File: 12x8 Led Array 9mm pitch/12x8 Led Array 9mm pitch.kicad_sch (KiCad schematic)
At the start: 25 parts, among them J1 LED ch 1-24, J2 LED ch 25-48, J3 LED ch 49-72, J4 LED ch 73-96, J5 logic/analog, U1 CD74HC4067M96, U2 CD74HC4067M96, U3 CD74HC4067M96, U4 CD74HC4067M96, U5 CD74HC4067M96, U6 CD74HC4067M96

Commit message: Swap to 6x 40-pin IDC ribbons (IDE-safe pinout), clear routing for rearrange
- J1-J6 both boards: 16 channels each = one PCA9685 bank per cable;
  pairs on pins 1-18/21-34, pin 20 NC (IDE key), GND 19+35-40
- Logic ribbon renamed J9; control screw terminal now J12
- Schematics regenerated (netlists verified 300+412), CONNECTIONS
  updated; connectors placed at nominal spots for user rearrangement
- All routing cleared except LED thermal via farms per user request
- New vault note: What Every Part Does

Co-Authored-By: Claude Fable 5 <noreply@anthropic.com>
Claude-Session: https://claude.ai/code/session_017oD54uh7Tvu54u9NPQNcZB
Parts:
- added J6: LED ch 81-96, Connector_IDC:IDC-Header_2x20_P2.54mm_Vertical, symbol Connector_Generic:Conn_02x20_Odd_Even
- added J9: logic/analog, Connector_IDC:IDC-Header_2x10_P2.54mm_Horizontal, symbol Connector_Generic:Conn_02x10_Odd_Even
- J1: value LED ch 1-24 -> LED ch 1-16; footprint Connector_IDC:IDC-Header_2x25_P2.54mm_Vertical -> Connector_IDC:IDC-Header_2x20_P2.54mm_Vertical; symbol Connector_Generic:Conn_02x25_Odd_Even -> Connector_Generic:Conn_02x20_Odd_Even; LCSC C9044 -> C9043
- J2: value LED ch 25-48 -> LED ch 17-32; footprint Connector_IDC:IDC-Header_2x25_P2.54mm_Vertical -> Connector_IDC:IDC-Header_2x20_P2.54mm_Vertical; symbol Connector_Generic:Conn_02x25_Odd_Even -> Connector_Generic:Conn_02x20_Odd_Even; LCSC C9044 -> C9043
- J3: value LED ch 49-72 -> LED ch 33-48; footprint Connector_IDC:IDC-Header_2x25_P2.54mm_Vertical -> Connector_IDC:IDC-Header_2x20_P2.54mm_Vertical; symbol Connector_Generic:Conn_02x25_Odd_Even -> Connector_Generic:Conn_02x20_Odd_Even; LCSC C9044 -> C9043
- J4: value LED ch 73-96 -> LED ch 49-64; footprint Connector_IDC:IDC-Header_2x25_P2.54mm_Vertical -> Connector_IDC:IDC-Header_2x20_P2.54mm_Vertical; symbol Connector_Generic:Conn_02x25_Odd_Even -> Connector_Generic:Conn_02x20_Odd_Even; LCSC C9044 -> C9043
- J5: value logic/analog -> LED ch 65-80; footprint Connector_IDC:IDC-Header_2x10_P2.54mm_Horizontal -> Connector_IDC:IDC-Header_2x20_P2.54mm_Vertical; symbol Connector_Generic:Conn_02x10_Odd_Even -> Connector_Generic:Conn_02x20_Odd_Even; LCSC C9144 -> C9043
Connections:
- net +3.3V: now also J9.1 (Pin_1); no longer J5.1 (Pin_1)
- net GND: now also J1.19 (Pin_19), J1.35 (Pin_35), J1.36 (Pin_36), J1.37 (Pin_37), J1.38 (Pin_38), J1.39 (Pin_39), J1.40 (Pin_40), J2.19 (Pin_19), J2.35 (Pin_35), J2.36 (Pin_36), J2.37 (Pin_37), J2.38 (Pin_38), J2.39 (Pin_39), J2.40 (Pin_40), J3.19 (Pin_19), J3.35 (Pin_35), J3.36 (Pin_36), J3.37 (Pin_37), J3.38 (Pin_38), J3.39 (Pin_39), J3.40 (Pin_40), J4.19 (Pin_19), J4.35 (Pin_35), J4.36 (Pin_36), J4.37 (Pin_37), J4.38 (Pin_38), J4.39 (Pin_39), J4.40 (Pin_40), J5.35 (Pin_35), J5.36 (Pin_36), J5.37 (Pin_37), J5.38 (Pin_38), J5.39 (Pin_39), J5.40 (Pin_40), J6.19 (Pin_19), J6.35 (Pin_35), J6.36 (Pin_36), J6.37 (Pin_37), J6.38 (Pin_38), J6.39 (Pin_39), J6.40 (Pin_40), J9.10 (Pin_10), J9.12 (Pin_12), J9.14 (Pin_14), J9.19 (Pin_19), J9.2 (Pin_2), J9.20 (Pin_20), J9.4 (Pin_4), J9.6 (Pin_6), J9.8 (Pin_8); no longer J1.49 (Pin_49), J1.50 (Pin_50), J2.49 (Pin_49), J2.50 (Pin_50), J3.49 (Pin_49), J3.50 (Pin_50), J4.49 (Pin_49), J4.50 (Pin_50), J5.10 (Pin_10), J5.12 (Pin_12), J5.14 (Pin_14), J5.2 (Pin_2), J5.20 (Pin_20), J5.4 (Pin_4), J5.6 (Pin_6), J5.8 (Pin_8)
- net LED_A10: now also J1.21 (Pin_21); no longer J2.25 (Pin_25)
- net LED_A11: now also J1.23 (Pin_23); no longer J2.33 (Pin_33)
- net LED_A12: now also J1.25 (Pin_25); no longer J2.41 (Pin_41)
- net LED_A13: now also J1.27 (Pin_27); no longer J1.3 (Pin_3)
- net LED_A14: now also J1.29 (Pin_29); no longer J1.11 (Pin_11)
- net LED_A15: now also J1.31 (Pin_31); no longer J1.19 (Pin_19)
- net LED_A16: now also J1.33 (Pin_33); no longer J1.27 (Pin_27)
- net LED_A17: now also J2.1 (Pin_1); no longer J1.35 (Pin_35)
- net LED_A18: now also J2.3 (Pin_3); no longer J1.43 (Pin_43)
- net LED_A19: now also J2.5 (Pin_5); no longer J2.3 (Pin_3)
- net LED_A2: now also J1.3 (Pin_3); no longer J1.9 (Pin_9)
- net LED_A20: now also J2.7 (Pin_7); no longer J2.11 (Pin_11)
- net LED_A21: now also J2.9 (Pin_9); no longer J2.19 (Pin_19)
- net LED_A22: now also J2.11 (Pin_11); no longer J2.27 (Pin_27)
- net LED_A23: now also J2.13 (Pin_13); no longer J2.35 (Pin_35)
- net LED_A24: now also J2.15 (Pin_15); no longer J2.43 (Pin_43)
- net LED_A25: now also J2.17 (Pin_17); no longer J1.5 (Pin_5)
- net LED_A26: now also J2.21 (Pin_21); no longer J1.13 (Pin_13)
- net LED_A27: now also J2.23 (Pin_23); no longer J1.21 (Pin_21)
- net LED_A28: now also J2.25 (Pin_25); no longer J1.29 (Pin_29)
- net LED_A29: now also J2.27 (Pin_27); no longer J1.37 (Pin_37)
- net LED_A3: now also J1.5 (Pin_5); no longer J1.17 (Pin_17)
- net LED_A30: now also J2.29 (Pin_29); no longer J1.45 (Pin_45)
- net LED_A31: now also J2.31 (Pin_31); no longer J2.5 (Pin_5)
- net LED_A32: now also J2.33 (Pin_33); no longer J2.13 (Pin_13)
- net LED_A33: now also J3.1 (Pin_1); no longer J2.21 (Pin_21)
- net LED_A34: now also J3.3 (Pin_3); no longer J2.29 (Pin_29)
- net LED_A35: now also J3.5 (Pin_5); no longer J2.37 (Pin_37)
- net LED_A36: now also J3.7 (Pin_7); no longer J2.45 (Pin_45)
- net LED_A37: now also J3.9 (Pin_9); no longer J1.7 (Pin_7)
- net LED_A38: now also J3.11 (Pin_11); no longer J1.15 (Pin_15)
- net LED_A39: now also J3.13 (Pin_13); no longer J1.23 (Pin_23)
- net LED_A4: now also J1.7 (Pin_7); no longer J1.25 (Pin_25)
- net LED_A40: now also J3.15 (Pin_15); no longer J1.31 (Pin_31)
- net LED_A41: now also J3.17 (Pin_17); no longer J1.39 (Pin_39)
- net LED_A42: now also J3.21 (Pin_21); no longer J1.47 (Pin_47)
- net LED_A43: now also J3.23 (Pin_23); no longer J2.7 (Pin_7)
- net LED_A44: now also J3.25 (Pin_25); no longer J2.15 (Pin_15)
- net LED_A45: now also J3.27 (Pin_27); no longer J2.23 (Pin_23)
- net LED_A46: now also J3.29 (Pin_29); no longer J2.31 (Pin_31)
- net LED_A47: now also J3.31 (Pin_31); no longer J2.39 (Pin_39)
- net LED_A48: now also J3.33 (Pin_33); no longer J2.47 (Pin_47)
- net LED_A5: now also J1.9 (Pin_9); no longer J1.33 (Pin_33)
- net LED_A50: now also J4.3 (Pin_3); no longer J4.9 (Pin_9)
- net LED_A51: now also J4.5 (Pin_5); no longer J4.17 (Pin_17)
- net LED_A52: now also J4.7 (Pin_7); no longer J4.25 (Pin_25)
- net LED_A53: now also J4.9 (Pin_9); no longer J4.33 (Pin_33)
- net LED_A54: now also J4.11 (Pin_11); no longer J4.41 (Pin_41)
- net LED_A55: now also J4.13 (Pin_13); no longer J3.1 (Pin_1)
- net LED_A56: now also J4.15 (Pin_15); no longer J3.9 (Pin_9)
- net LED_A57: now also J4.17 (Pin_17); no longer J3.17 (Pin_17)
- net LED_A58: now also J4.21 (Pin_21); no longer J3.25 (Pin_25)
- net LED_A59: now also J4.23 (Pin_23); no longer J3.33 (Pin_33)
- net LED_A6: now also J1.11 (Pin_11); no longer J1.41 (Pin_41)
- net LED_A60: now also J4.25 (Pin_25); no longer J3.41 (Pin_41)
- net LED_A61: now also J4.27 (Pin_27); no longer J4.3 (Pin_3)
- net LED_A62: now also J4.29 (Pin_29); no longer J4.11 (Pin_11)
- net LED_A63: now also J4.31 (Pin_31); no longer J4.19 (Pin_19)
- net LED_A64: now also J4.33 (Pin_33); no longer J4.27 (Pin_27)
- net LED_A65: now also J5.1 (Pin_1); no longer J4.35 (Pin_35)
- net LED_A66: now also J5.3 (Pin_3); no longer J4.43 (Pin_43)
- net LED_A67: now also J5.5 (Pin_5); no longer J3.3 (Pin_3)
- net LED_A68: now also J5.7 (Pin_7); no longer J3.11 (Pin_11)
- net LED_A69: now also J5.9 (Pin_9); no longer J3.19 (Pin_19)
- net LED_A7: now also J1.13 (Pin_13); no longer J2.1 (Pin_1)
- net LED_A70: now also J5.11 (Pin_11); no longer J3.27 (Pin_27)
- net LED_A71: now also J5.13 (Pin_13); no longer J3.35 (Pin_35)
- net LED_A72: now also J5.15 (Pin_15); no longer J3.43 (Pin_43)
- net LED_A73: now also J5.17 (Pin_17); no longer J4.5 (Pin_5)
- net LED_A74: now also J5.21 (Pin_21); no longer J4.13 (Pin_13)
- net LED_A75: now also J5.23 (Pin_23); no longer J4.21 (Pin_21)
- net LED_A76: now also J5.25 (Pin_25); no longer J4.29 (Pin_29)
- net LED_A77: now also J5.27 (Pin_27); no longer J4.37 (Pin_37)
- net LED_A78: now also J5.29 (Pin_29); no longer J4.45 (Pin_45)
- net LED_A79: now also J5.31 (Pin_31); no longer J3.5 (Pin_5)
- net LED_A8: now also J1.15 (Pin_15); no longer J2.9 (Pin_9)
- net LED_A80: now also J5.33 (Pin_33); no longer J3.13 (Pin_13)
- net LED_A81: now also J6.1 (Pin_1); no longer J3.21 (Pin_21)
- net LED_A82: now also J6.3 (Pin_3); no longer J3.29 (Pin_29)
- net LED_A83: now also J6.5 (Pin_5); no longer J3.37 (Pin_37)
- net LED_A84: now also J6.7 (Pin_7); no longer J3.45 (Pin_45)
- net LED_A85: now also J6.9 (Pin_9); no longer J4.7 (Pin_7)
- net LED_A86: now also J6.11 (Pin_11); no longer J4.15 (Pin_15)
- net LED_A87: now also J6.13 (Pin_13); no longer J4.23 (Pin_23)
- net LED_A88: now also J6.15 (Pin_15); no longer J4.31 (Pin_31)
- net LED_A89: now also J6.17 (Pin_17); no longer J4.39 (Pin_39)
- net LED_A9: now also J1.17 (Pin_17); no longer J2.17 (Pin_17)
- net LED_A90: now also J6.21 (Pin_21); no longer J4.47 (Pin_47)
- net LED_A91: now also J6.23 (Pin_23); no longer J3.7 (Pin_7)
- net LED_A92: now also J6.25 (Pin_25); no longer J3.15 (Pin_15)
- net LED_A93: now also J6.27 (Pin_27); no longer J3.23 (Pin_23)
- net LED_A94: now also J6.29 (Pin_29); no longer J3.31 (Pin_31)
- net LED_A95: now also J6.31 (Pin_31); no longer J3.39 (Pin_39)
- net LED_A96: now also J6.33 (Pin_33); no longer J3.47 (Pin_47)
- net LED_K10: now also J1.22 (Pin_22); no longer J2.26 (Pin_26)
- net LED_K11: now also J1.24 (Pin_24); no longer J2.34 (Pin_34)
- net LED_K12: now also J1.26 (Pin_26); no longer J2.42 (Pin_42)
- net LED_K13: now also J1.28 (Pin_28); no longer J1.4 (Pin_4)
- net LED_K14: now also J1.30 (Pin_30); no longer J1.12 (Pin_12)
- net LED_K15: now also J1.32 (Pin_32); no longer J1.20 (Pin_20)
- net LED_K16: now also J1.34 (Pin_34); no longer J1.28 (Pin_28)
- net LED_K17: now also J2.2 (Pin_2); no longer J1.36 (Pin_36)
- net LED_K18: now also J2.4 (Pin_4); no longer J1.44 (Pin_44)
- net LED_K19: now also J2.6 (Pin_6); no longer J2.4 (Pin_4)
- net LED_K2: now also J1.4 (Pin_4); no longer J1.10 (Pin_10)
- net LED_K20: now also J2.8 (Pin_8); no longer J2.12 (Pin_12)
- net LED_K21: now also J2.10 (Pin_10); no longer J2.20 (Pin_20)
- net LED_K22: now also J2.12 (Pin_12); no longer J2.28 (Pin_28)
- net LED_K23: now also J2.14 (Pin_14); no longer J2.36 (Pin_36)
- net LED_K24: now also J2.16 (Pin_16); no longer J2.44 (Pin_44)
- net LED_K25: now also J2.18 (Pin_18); no longer J1.6 (Pin_6)
- net LED_K26: now also J2.22 (Pin_22); no longer J1.14 (Pin_14)
- net LED_K27: now also J2.24 (Pin_24); no longer J1.22 (Pin_22)
- net LED_K28: now also J2.26 (Pin_26); no longer J1.30 (Pin_30)
- net LED_K29: now also J2.28 (Pin_28); no longer J1.38 (Pin_38)
- net LED_K3: now also J1.6 (Pin_6); no longer J1.18 (Pin_18)
- net LED_K30: now also J2.30 (Pin_30); no longer J1.46 (Pin_46)
- net LED_K31: now also J2.32 (Pin_32); no longer J2.6 (Pin_6)
- net LED_K32: now also J2.34 (Pin_34); no longer J2.14 (Pin_14)
- net LED_K33: now also J3.2 (Pin_2); no longer J2.22 (Pin_22)
- net LED_K34: now also J3.4 (Pin_4); no longer J2.30 (Pin_30)
- net LED_K35: now also J3.6 (Pin_6); no longer J2.38 (Pin_38)
- net LED_K36: now also J3.8 (Pin_8); no longer J2.46 (Pin_46)
- net LED_K37: now also J3.10 (Pin_10); no longer J1.8 (Pin_8)
- net LED_K38: now also J3.12 (Pin_12); no longer J1.16 (Pin_16)
- net LED_K39: now also J3.14 (Pin_14); no longer J1.24 (Pin_24)
- net LED_K4: now also J1.8 (Pin_8); no longer J1.26 (Pin_26)
- net LED_K40: now also J3.16 (Pin_16); no longer J1.32 (Pin_32)
- net LED_K41: now also J3.18 (Pin_18); no longer J1.40 (Pin_40)
- net LED_K42: now also J3.22 (Pin_22); no longer J1.48 (Pin_48)
- net LED_K43: now also J3.24 (Pin_24); no longer J2.8 (Pin_8)
- net LED_K44: now also J3.26 (Pin_26); no longer J2.16 (Pin_16)
- net LED_K45: now also J3.28 (Pin_28); no longer J2.24 (Pin_24)
- net LED_K46: now also J3.30 (Pin_30); no longer J2.32 (Pin_32)
- net LED_K47: now also J3.32 (Pin_32); no longer J2.40 (Pin_40)
- net LED_K48: now also J3.34 (Pin_34); no longer J2.48 (Pin_48)
- net LED_K5: now also J1.10 (Pin_10); no longer J1.34 (Pin_34)
- net LED_K50: now also J4.4 (Pin_4); no longer J4.10 (Pin_10)
- net LED_K51: now also J4.6 (Pin_6); no longer J4.18 (Pin_18)
- net LED_K52: now also J4.8 (Pin_8); no longer J4.26 (Pin_26)
- net LED_K53: now also J4.10 (Pin_10); no longer J4.34 (Pin_34)
- net LED_K54: now also J4.12 (Pin_12); no longer J4.42 (Pin_42)
- net LED_K55: now also J4.14 (Pin_14); no longer J3.2 (Pin_2)
- net LED_K56: now also J4.16 (Pin_16); no longer J3.10 (Pin_10)
- net LED_K57: now also J4.18 (Pin_18); no longer J3.18 (Pin_18)
- net LED_K58: now also J4.22 (Pin_22); no longer J3.26 (Pin_26)
- net LED_K59: now also J4.24 (Pin_24); no longer J3.34 (Pin_34)
- net LED_K6: now also J1.12 (Pin_12); no longer J1.42 (Pin_42)
- net LED_K60: now also J4.26 (Pin_26); no longer J3.42 (Pin_42)
- net LED_K61: now also J4.28 (Pin_28); no longer J4.4 (Pin_4)
- net LED_K62: now also J4.30 (Pin_30); no longer J4.12 (Pin_12)
- net LED_K63: now also J4.32 (Pin_32); no longer J4.20 (Pin_20)
- net LED_K64: now also J4.34 (Pin_34); no longer J4.28 (Pin_28)
- net LED_K65: now also J5.2 (Pin_2); no longer J4.36 (Pin_36)
- net LED_K66: now also J5.4 (Pin_4); no longer J4.44 (Pin_44)
- net LED_K67: now also J5.6 (Pin_6); no longer J3.4 (Pin_4)
- net LED_K68: now also J5.8 (Pin_8); no longer J3.12 (Pin_12)
- net LED_K69: now also J5.10 (Pin_10); no longer J3.20 (Pin_20)
- net LED_K7: now also J1.14 (Pin_14); no longer J2.2 (Pin_2)
- net LED_K70: now also J5.12 (Pin_12); no longer J3.28 (Pin_28)
- net LED_K71: now also J5.14 (Pin_14); no longer J3.36 (Pin_36)
- net LED_K72: now also J5.16 (Pin_16); no longer J3.44 (Pin_44)
- net LED_K73: now also J5.18 (Pin_18); no longer J4.6 (Pin_6)
- net LED_K74: now also J5.22 (Pin_22); no longer J4.14 (Pin_14)
- net LED_K75: now also J5.24 (Pin_24); no longer J4.22 (Pin_22)
- net LED_K76: now also J5.26 (Pin_26); no longer J4.30 (Pin_30)
- net LED_K77: now also J5.28 (Pin_28); no longer J4.38 (Pin_38)
- net LED_K78: now also J5.30 (Pin_30); no longer J4.46 (Pin_46)
- net LED_K79: now also J5.32 (Pin_32); no longer J3.6 (Pin_6)
- net LED_K8: now also J1.16 (Pin_16); no longer J2.10 (Pin_10)
- net LED_K80: now also J5.34 (Pin_34); no longer J3.14 (Pin_14)
- net LED_K81: now also J6.2 (Pin_2); no longer J3.22 (Pin_22)
- net LED_K82: now also J6.4 (Pin_4); no longer J3.30 (Pin_30)
- net LED_K83: now also J6.6 (Pin_6); no longer J3.38 (Pin_38)
- net LED_K84: now also J6.8 (Pin_8); no longer J3.46 (Pin_46)
- net LED_K85: now also J6.10 (Pin_10); no longer J4.8 (Pin_8)
- net LED_K86: now also J6.12 (Pin_12); no longer J4.16 (Pin_16)
- net LED_K87: now also J6.14 (Pin_14); no longer J4.24 (Pin_24)
- net LED_K88: now also J6.16 (Pin_16); no longer J4.32 (Pin_32)
- net LED_K89: now also J6.18 (Pin_18); no longer J4.40 (Pin_40)
- net LED_K9: now also J1.18 (Pin_18); no longer J2.18 (Pin_18)
- net LED_K90: now also J6.22 (Pin_22); no longer J4.48 (Pin_48)
- net LED_K91: now also J6.24 (Pin_24); no longer J3.8 (Pin_8)
- net LED_K92: now also J6.26 (Pin_26); no longer J3.16 (Pin_16)
- net LED_K93: now also J6.28 (Pin_28); no longer J3.24 (Pin_24)
- net LED_K94: now also J6.30 (Pin_30); no longer J3.32 (Pin_32)
- net LED_K95: now also J6.32 (Pin_32); no longer J3.40 (Pin_40)
- net LED_K96: now also J6.34 (Pin_34); no longer J3.48 (Pin_48)
- net MUX_A0: now also J9.15 (Pin_15); no longer J5.15 (Pin_15)
- net MUX_A1: now also J9.16 (Pin_16); no longer J5.16 (Pin_16)
- net MUX_A2: now also J9.17 (Pin_17); no longer J5.17 (Pin_17)
- net MUX_A3: now also J9.18 (Pin_18); no longer J5.18 (Pin_18)
- net NTC_SIG1: now also J9.3 (Pin_3); no longer J5.3 (Pin_3)
- net NTC_SIG2: now also J9.5 (Pin_5); no longer J5.5 (Pin_5)
- net NTC_SIG3: now also J9.7 (Pin_7); no longer J5.7 (Pin_7)
- net NTC_SIG4: now also J9.9 (Pin_9); no longer J5.9 (Pin_9)
- net NTC_SIG5: now also J9.11 (Pin_11); no longer J5.11 (Pin_11)
- net NTC_SIG6: now also J9.13 (Pin_13); no longer J5.13 (Pin_13)
- no-connect marks 0 -> 6
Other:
- moved on the sheet: C1, H1, H2, H3, H4, H5, TP1, TP2, TP3, U1, U2, U3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

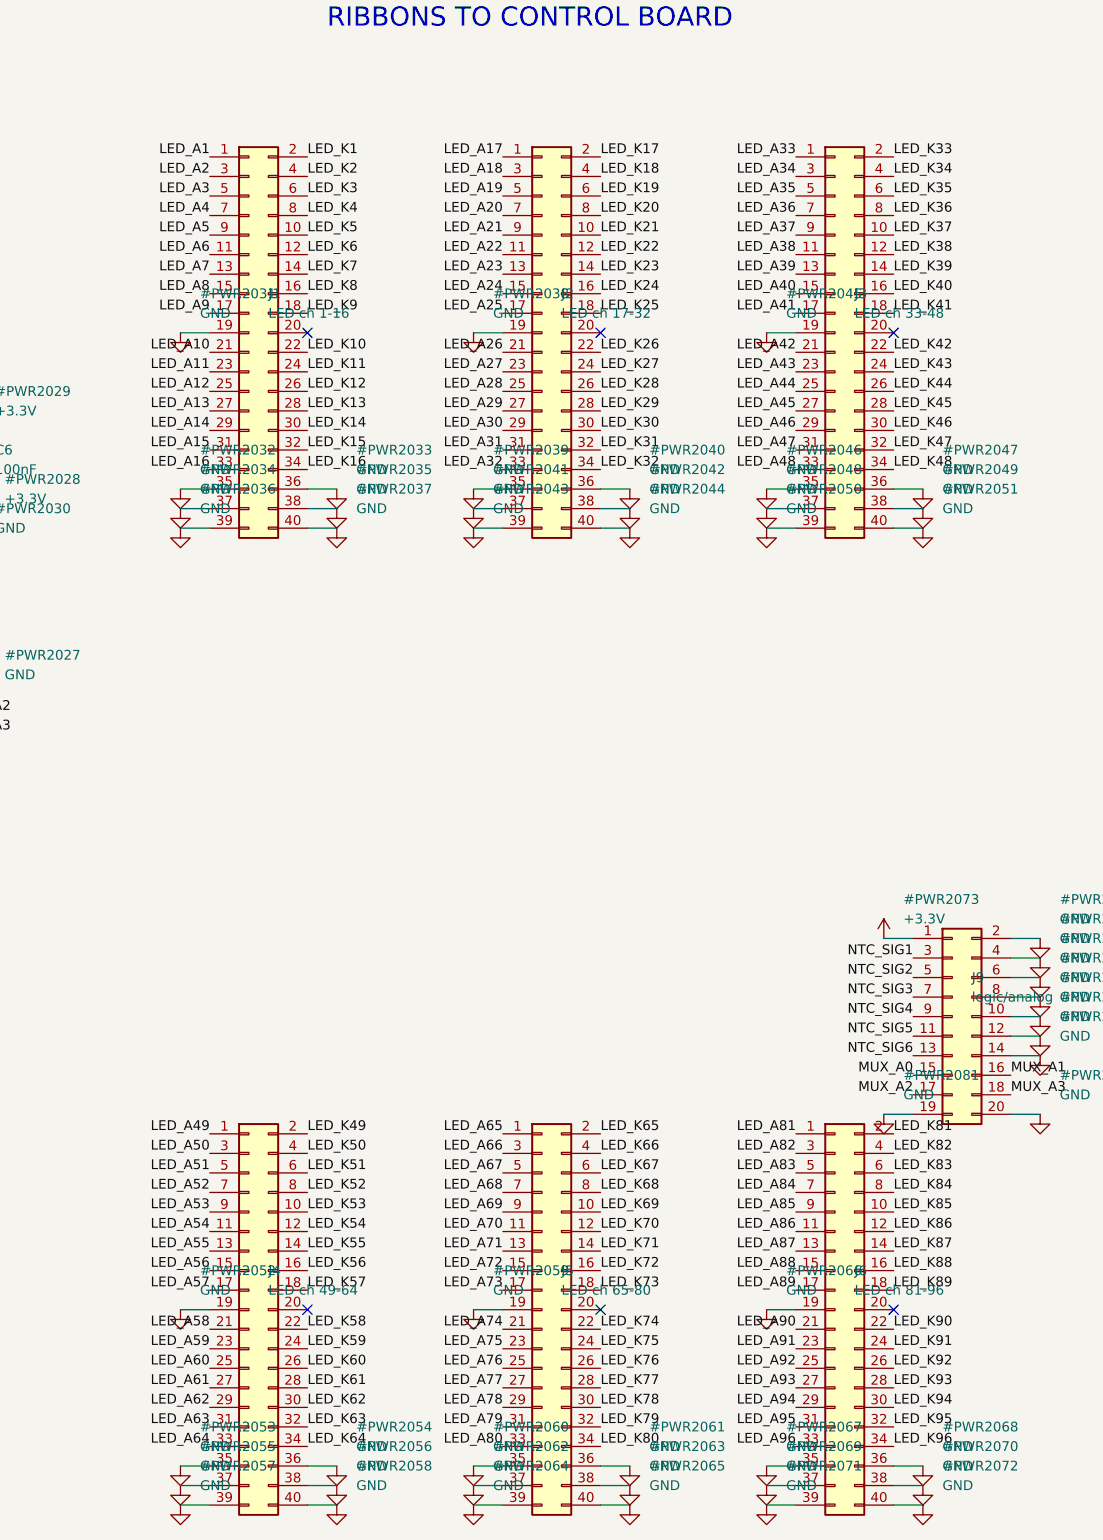
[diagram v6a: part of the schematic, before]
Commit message: Driver-board pinout optimization from user's rearranged placement
- CONN_MAP: per-ribbon pair order jointly optimized against BOTH
  boards' geometry (pads projected on connector axes, combined rank)
- PCA_MAP: each PCA9685's 16 outputs assigned to its bank's DIM
  lines by physical order (crossing-free fan-out)
- design_data table-driven; schematics regenerated; netlists verify
  (300+412); pads re-netted on both boards; CONNECTIONS updated

Co-Authored-By: Claude Fable 5 <noreply@anthropic.com>
Claude-Session: https://claude.ai/code/session_017oD54uh7Tvu54u9NPQNcZB
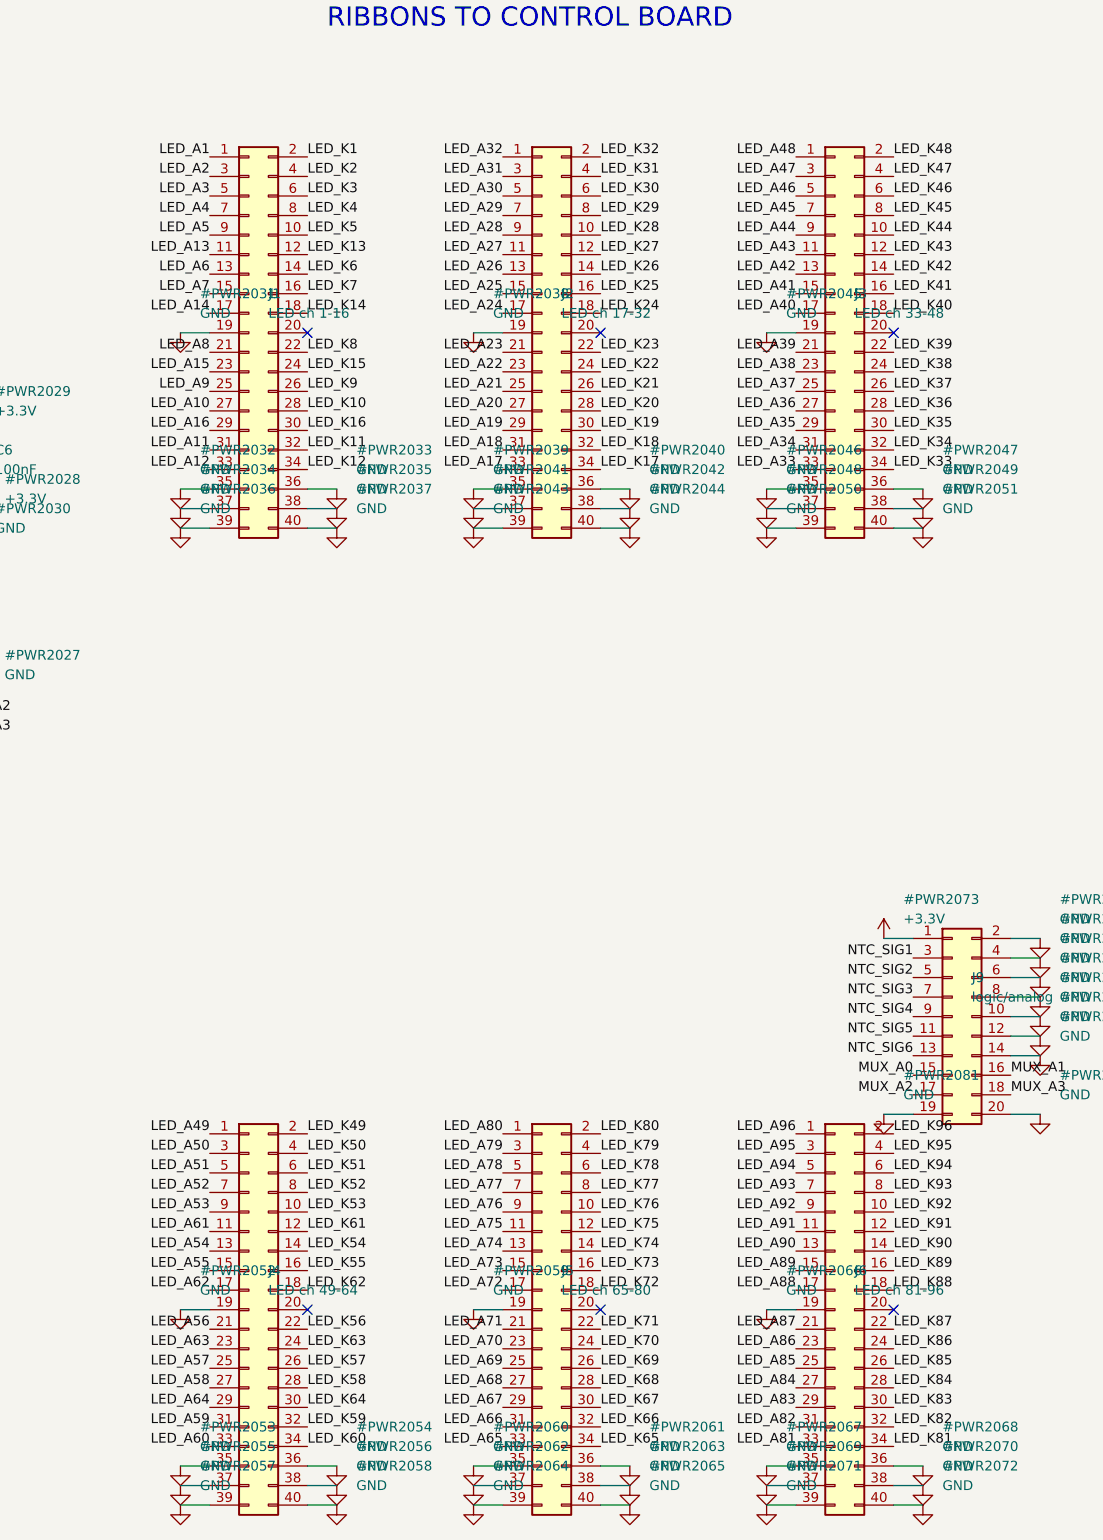
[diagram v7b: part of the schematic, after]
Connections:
- net LED_A10: now also J1.27 (Pin_27); no longer J1.21 (Pin_21)
- net LED_A11: now also J1.31 (Pin_31); no longer J1.23 (Pin_23)
- net LED_A12: now also J1.33 (Pin_33); no longer J1.25 (Pin_25)
- net LED_A13: now also J1.11 (Pin_11); no longer J1.27 (Pin_27)
- net LED_A14: now also J1.17 (Pin_17); no longer J1.29 (Pin_29)
- net LED_A15: now also J1.23 (Pin_23); no longer J1.31 (Pin_31)
- net LED_A16: now also J1.29 (Pin_29); no longer J1.33 (Pin_33)
- net LED_A17: now also J2.33 (Pin_33); no longer J2.1 (Pin_1)
- net LED_A18: now also J2.31 (Pin_31); no longer J2.3 (Pin_3)
- net LED_A19: now also J2.29 (Pin_29); no longer J2.5 (Pin_5)
- net LED_A20: now also J2.27 (Pin_27); no longer J2.7 (Pin_7)
- net LED_A21: now also J2.25 (Pin_25); no longer J2.9 (Pin_9)
- net LED_A22: now also J2.23 (Pin_23); no longer J2.11 (Pin_11)
- net LED_A23: now also J2.21 (Pin_21); no longer J2.13 (Pin_13)
- net LED_A24: now also J2.17 (Pin_17); no longer J2.15 (Pin_15)
- net LED_A25: now also J2.15 (Pin_15); no longer J2.17 (Pin_17)
- net LED_A26: now also J2.13 (Pin_13); no longer J2.21 (Pin_21)
- net LED_A27: now also J2.11 (Pin_11); no longer J2.23 (Pin_23)
- net LED_A28: now also J2.9 (Pin_9); no longer J2.25 (Pin_25)
- net LED_A29: now also J2.7 (Pin_7); no longer J2.27 (Pin_27)
- net LED_A30: now also J2.5 (Pin_5); no longer J2.29 (Pin_29)
- net LED_A31: now also J2.3 (Pin_3); no longer J2.31 (Pin_31)
- net LED_A32: now also J2.1 (Pin_1); no longer J2.33 (Pin_33)
- net LED_A33: now also J3.33 (Pin_33); no longer J3.1 (Pin_1)
- net LED_A34: now also J3.31 (Pin_31); no longer J3.3 (Pin_3)
- net LED_A35: now also J3.29 (Pin_29); no longer J3.5 (Pin_5)
- net LED_A36: now also J3.27 (Pin_27); no longer J3.7 (Pin_7)
- net LED_A37: now also J3.25 (Pin_25); no longer J3.9 (Pin_9)
- net LED_A38: now also J3.23 (Pin_23); no longer J3.11 (Pin_11)
- net LED_A39: now also J3.21 (Pin_21); no longer J3.13 (Pin_13)
- net LED_A40: now also J3.17 (Pin_17); no longer J3.15 (Pin_15)
- net LED_A41: now also J3.15 (Pin_15); no longer J3.17 (Pin_17)
- net LED_A42: now also J3.13 (Pin_13); no longer J3.21 (Pin_21)
- net LED_A43: now also J3.11 (Pin_11); no longer J3.23 (Pin_23)
- net LED_A44: now also J3.9 (Pin_9); no longer J3.25 (Pin_25)
- net LED_A45: now also J3.7 (Pin_7); no longer J3.27 (Pin_27)
- net LED_A46: now also J3.5 (Pin_5); no longer J3.29 (Pin_29)
- net LED_A47: now also J3.3 (Pin_3); no longer J3.31 (Pin_31)
- net LED_A48: now also J3.1 (Pin_1); no longer J3.33 (Pin_33)
- net LED_A54: now also J4.13 (Pin_13); no longer J4.11 (Pin_11)
- net LED_A55: now also J4.15 (Pin_15); no longer J4.13 (Pin_13)
- net LED_A56: now also J4.21 (Pin_21); no longer J4.15 (Pin_15)
- net LED_A57: now also J4.25 (Pin_25); no longer J4.17 (Pin_17)
- net LED_A58: now also J4.27 (Pin_27); no longer J4.21 (Pin_21)
- net LED_A59: now also J4.31 (Pin_31); no longer J4.23 (Pin_23)
- net LED_A6: now also J1.13 (Pin_13); no longer J1.11 (Pin_11)
- net LED_A60: now also J4.33 (Pin_33); no longer J4.25 (Pin_25)
- net LED_A61: now also J4.11 (Pin_11); no longer J4.27 (Pin_27)
- net LED_A62: now also J4.17 (Pin_17); no longer J4.29 (Pin_29)
- net LED_A63: now also J4.23 (Pin_23); no longer J4.31 (Pin_31)
- net LED_A64: now also J4.29 (Pin_29); no longer J4.33 (Pin_33)
- net LED_A65: now also J5.33 (Pin_33); no longer J5.1 (Pin_1)
- net LED_A66: now also J5.31 (Pin_31); no longer J5.3 (Pin_3)
- net LED_A67: now also J5.29 (Pin_29); no longer J5.5 (Pin_5)
- net LED_A68: now also J5.27 (Pin_27); no longer J5.7 (Pin_7)
- net LED_A69: now also J5.25 (Pin_25); no longer J5.9 (Pin_9)
- net LED_A7: now also J1.15 (Pin_15); no longer J1.13 (Pin_13)
- net LED_A70: now also J5.23 (Pin_23); no longer J5.11 (Pin_11)
- net LED_A71: now also J5.21 (Pin_21); no longer J5.13 (Pin_13)
- net LED_A72: now also J5.17 (Pin_17); no longer J5.15 (Pin_15)
- net LED_A73: now also J5.15 (Pin_15); no longer J5.17 (Pin_17)
- net LED_A74: now also J5.13 (Pin_13); no longer J5.21 (Pin_21)
- net LED_A75: now also J5.11 (Pin_11); no longer J5.23 (Pin_23)
- net LED_A76: now also J5.9 (Pin_9); no longer J5.25 (Pin_25)
- net LED_A77: now also J5.7 (Pin_7); no longer J5.27 (Pin_27)
- net LED_A78: now also J5.5 (Pin_5); no longer J5.29 (Pin_29)
- net LED_A79: now also J5.3 (Pin_3); no longer J5.31 (Pin_31)
- net LED_A8: now also J1.21 (Pin_21); no longer J1.15 (Pin_15)
- net LED_A80: now also J5.1 (Pin_1); no longer J5.33 (Pin_33)
- net LED_A81: now also J6.33 (Pin_33); no longer J6.1 (Pin_1)
- net LED_A82: now also J6.31 (Pin_31); no longer J6.3 (Pin_3)
- net LED_A83: now also J6.29 (Pin_29); no longer J6.5 (Pin_5)
- net LED_A84: now also J6.27 (Pin_27); no longer J6.7 (Pin_7)
- net LED_A85: now also J6.25 (Pin_25); no longer J6.9 (Pin_9)
- net LED_A86: now also J6.23 (Pin_23); no longer J6.11 (Pin_11)
- net LED_A87: now also J6.21 (Pin_21); no longer J6.13 (Pin_13)
- net LED_A88: now also J6.17 (Pin_17); no longer J6.15 (Pin_15)
- net LED_A89: now also J6.15 (Pin_15); no longer J6.17 (Pin_17)
- net LED_A9: now also J1.25 (Pin_25); no longer J1.17 (Pin_17)
- net LED_A90: now also J6.13 (Pin_13); no longer J6.21 (Pin_21)
- net LED_A91: now also J6.11 (Pin_11); no longer J6.23 (Pin_23)
- net LED_A92: now also J6.9 (Pin_9); no longer J6.25 (Pin_25)
- net LED_A93: now also J6.7 (Pin_7); no longer J6.27 (Pin_27)
- net LED_A94: now also J6.5 (Pin_5); no longer J6.29 (Pin_29)
- net LED_A95: now also J6.3 (Pin_3); no longer J6.31 (Pin_31)
- net LED_A96: now also J6.1 (Pin_1); no longer J6.33 (Pin_33)
- net LED_K10: now also J1.28 (Pin_28); no longer J1.22 (Pin_22)
- net LED_K11: now also J1.32 (Pin_32); no longer J1.24 (Pin_24)
- net LED_K12: now also J1.34 (Pin_34); no longer J1.26 (Pin_26)
- net LED_K13: now also J1.12 (Pin_12); no longer J1.28 (Pin_28)
- net LED_K14: now also J1.18 (Pin_18); no longer J1.30 (Pin_30)
- net LED_K15: now also J1.24 (Pin_24); no longer J1.32 (Pin_32)
- net LED_K16: now also J1.30 (Pin_30); no longer J1.34 (Pin_34)
- net LED_K17: now also J2.34 (Pin_34); no longer J2.2 (Pin_2)
- net LED_K18: now also J2.32 (Pin_32); no longer J2.4 (Pin_4)
- net LED_K19: now also J2.30 (Pin_30); no longer J2.6 (Pin_6)
- net LED_K20: now also J2.28 (Pin_28); no longer J2.8 (Pin_8)
- net LED_K21: now also J2.26 (Pin_26); no longer J2.10 (Pin_10)
- net LED_K22: now also J2.24 (Pin_24); no longer J2.12 (Pin_12)
- net LED_K23: now also J2.22 (Pin_22); no longer J2.14 (Pin_14)
- net LED_K24: now also J2.18 (Pin_18); no longer J2.16 (Pin_16)
- net LED_K25: now also J2.16 (Pin_16); no longer J2.18 (Pin_18)
- net LED_K26: now also J2.14 (Pin_14); no longer J2.22 (Pin_22)
- net LED_K27: now also J2.12 (Pin_12); no longer J2.24 (Pin_24)
- net LED_K28: now also J2.10 (Pin_10); no longer J2.26 (Pin_26)
- net LED_K29: now also J2.8 (Pin_8); no longer J2.28 (Pin_28)
- net LED_K30: now also J2.6 (Pin_6); no longer J2.30 (Pin_30)
- net LED_K31: now also J2.4 (Pin_4); no longer J2.32 (Pin_32)
- net LED_K32: now also J2.2 (Pin_2); no longer J2.34 (Pin_34)
- net LED_K33: now also J3.34 (Pin_34); no longer J3.2 (Pin_2)
- net LED_K34: now also J3.32 (Pin_32); no longer J3.4 (Pin_4)
- net LED_K35: now also J3.30 (Pin_30); no longer J3.6 (Pin_6)
- net LED_K36: now also J3.28 (Pin_28); no longer J3.8 (Pin_8)
- net LED_K37: now also J3.26 (Pin_26); no longer J3.10 (Pin_10)
- net LED_K38: now also J3.24 (Pin_24); no longer J3.12 (Pin_12)
- net LED_K39: now also J3.22 (Pin_22); no longer J3.14 (Pin_14)
- net LED_K40: now also J3.18 (Pin_18); no longer J3.16 (Pin_16)
- net LED_K41: now also J3.16 (Pin_16); no longer J3.18 (Pin_18)
- net LED_K42: now also J3.14 (Pin_14); no longer J3.22 (Pin_22)
- net LED_K43: now also J3.12 (Pin_12); no longer J3.24 (Pin_24)
- net LED_K44: now also J3.10 (Pin_10); no longer J3.26 (Pin_26)
- net LED_K45: now also J3.8 (Pin_8); no longer J3.28 (Pin_28)
- net LED_K46: now also J3.6 (Pin_6); no longer J3.30 (Pin_30)
- net LED_K47: now also J3.4 (Pin_4); no longer J3.32 (Pin_32)
- net LED_K48: now also J3.2 (Pin_2); no longer J3.34 (Pin_34)
- net LED_K54: now also J4.14 (Pin_14); no longer J4.12 (Pin_12)
- net LED_K55: now also J4.16 (Pin_16); no longer J4.14 (Pin_14)
- net LED_K56: now also J4.22 (Pin_22); no longer J4.16 (Pin_16)
- net LED_K57: now also J4.26 (Pin_26); no longer J4.18 (Pin_18)
- net LED_K58: now also J4.28 (Pin_28); no longer J4.22 (Pin_22)
- net LED_K59: now also J4.32 (Pin_32); no longer J4.24 (Pin_24)
- net LED_K6: now also J1.14 (Pin_14); no longer J1.12 (Pin_12)
- net LED_K60: now also J4.34 (Pin_34); no longer J4.26 (Pin_26)
- net LED_K61: now also J4.12 (Pin_12); no longer J4.28 (Pin_28)
- net LED_K62: now also J4.18 (Pin_18); no longer J4.30 (Pin_30)
- net LED_K63: now also J4.24 (Pin_24); no longer J4.32 (Pin_32)
- net LED_K64: now also J4.30 (Pin_30); no longer J4.34 (Pin_34)
- net LED_K65: now also J5.34 (Pin_34); no longer J5.2 (Pin_2)
- net LED_K66: now also J5.32 (Pin_32); no longer J5.4 (Pin_4)
- net LED_K67: now also J5.30 (Pin_30); no longer J5.6 (Pin_6)
- net LED_K68: now also J5.28 (Pin_28); no longer J5.8 (Pin_8)
- net LED_K69: now also J5.26 (Pin_26); no longer J5.10 (Pin_10)
- net LED_K7: now also J1.16 (Pin_16); no longer J1.14 (Pin_14)
- net LED_K70: now also J5.24 (Pin_24); no longer J5.12 (Pin_12)
- net LED_K71: now also J5.22 (Pin_22); no longer J5.14 (Pin_14)
- net LED_K72: now also J5.18 (Pin_18); no longer J5.16 (Pin_16)
- net LED_K73: now also J5.16 (Pin_16); no longer J5.18 (Pin_18)
- net LED_K74: now also J5.14 (Pin_14); no longer J5.22 (Pin_22)
- net LED_K75: now also J5.12 (Pin_12); no longer J5.24 (Pin_24)
- net LED_K76: now also J5.10 (Pin_10); no longer J5.26 (Pin_26)
- net LED_K77: now also J5.8 (Pin_8); no longer J5.28 (Pin_28)
- net LED_K78: now also J5.6 (Pin_6); no longer J5.30 (Pin_30)
- net LED_K79: now also J5.4 (Pin_4); no longer J5.32 (Pin_32)
- net LED_K8: now also J1.22 (Pin_22); no longer J1.16 (Pin_16)
- net LED_K80: now also J5.2 (Pin_2); no longer J5.34 (Pin_34)
- net LED_K81: now also J6.34 (Pin_34); no longer J6.2 (Pin_2)
- net LED_K82: now also J6.32 (Pin_32); no longer J6.4 (Pin_4)
- net LED_K83: now also J6.30 (Pin_30); no longer J6.6 (Pin_6)
- net LED_K84: now also J6.28 (Pin_28); no longer J6.8 (Pin_8)
- net LED_K85: now also J6.26 (Pin_26); no longer J6.10 (Pin_10)
- net LED_K86: now also J6.24 (Pin_24); no longer J6.12 (Pin_12)
- net LED_K87: now also J6.22 (Pin_22); no longer J6.14 (Pin_14)
- net LED_K88: now also J6.18 (Pin_18); no longer J6.16 (Pin_16)
- net LED_K89: now also J6.16 (Pin_16); no longer J6.18 (Pin_18)
- net LED_K9: now also J1.26 (Pin_26); no longer J1.18 (Pin_18)
- net LED_K90: now also J6.14 (Pin_14); no longer J6.22 (Pin_22)
- net LED_K91: now also J6.12 (Pin_12); no longer J6.24 (Pin_24)
- net LED_K92: now also J6.10 (Pin_10); no longer J6.26 (Pin_26)
- net LED_K93: now also J6.8 (Pin_8); no longer J6.28 (Pin_28)
- net LED_K94: now also J6.6 (Pin_6); no longer J6.30 (Pin_30)
- net LED_K95: now also J6.4 (Pin_4); no longer J6.32 (Pin_32)
- net LED_K96: now also J6.2 (Pin_2); no longer J6.34 (Pin_34)
